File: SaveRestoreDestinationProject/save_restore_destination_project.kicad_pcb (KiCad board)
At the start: 2 copper layers, 21 parts

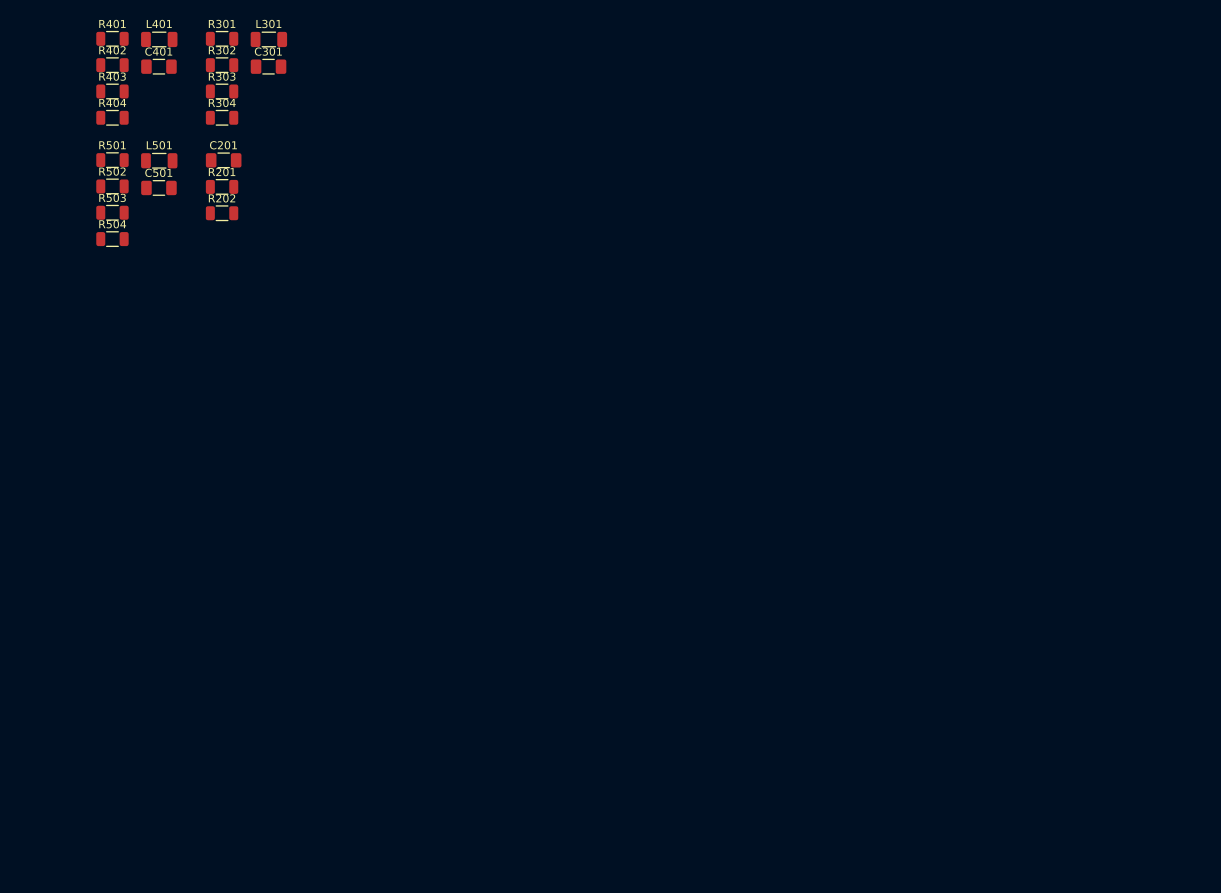
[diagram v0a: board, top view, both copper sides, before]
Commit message: Add support for connected drawings, update test template
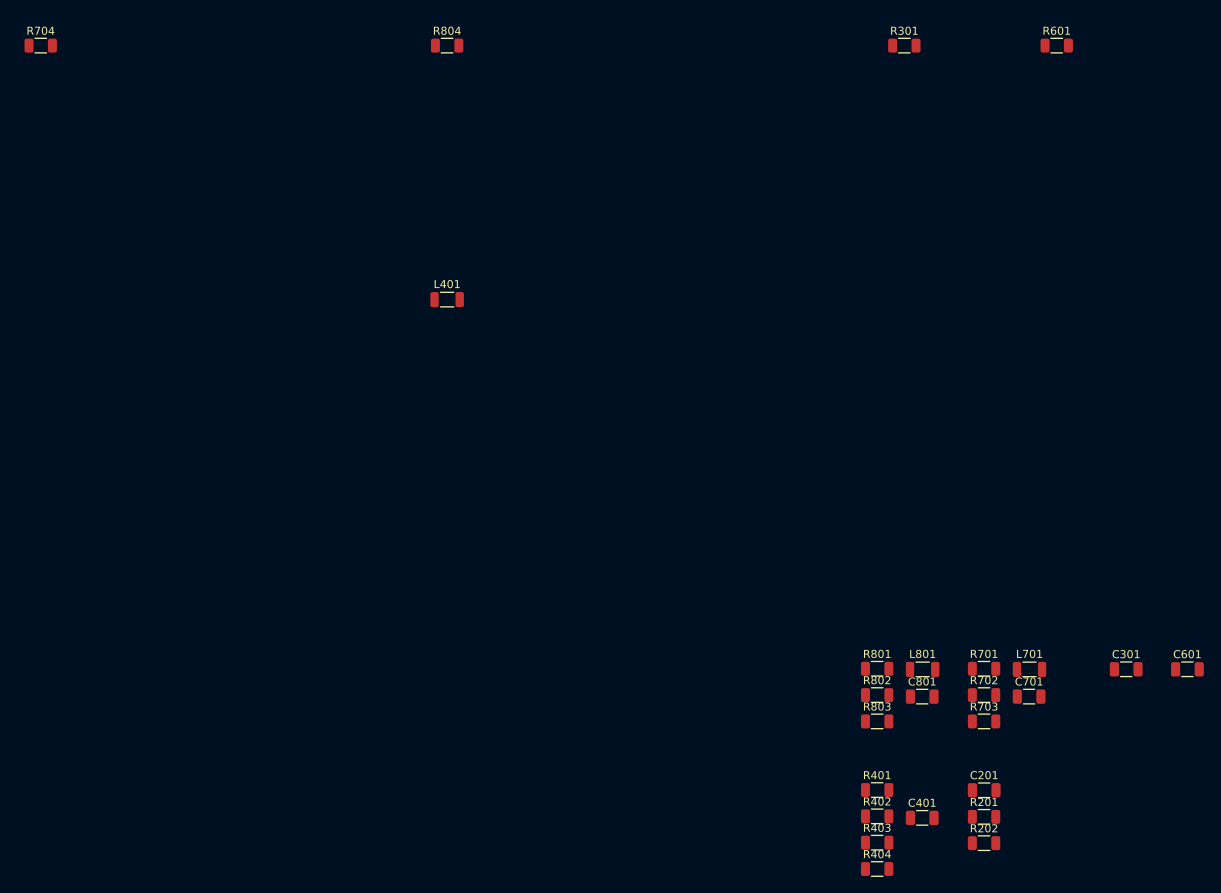
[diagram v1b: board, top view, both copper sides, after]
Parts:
- removed C501: 100n, Capacitor_SMD:C_1206_3216Metric_Pad1.33x1.80mm_HandSolder
- removed L301, L501: 10uH, Inductor_SMD:L_1206_3216Metric_Pad1.22x1.90mm_HandSolder
- removed R302, R502: 4k7, Resistor_SMD:R_1206_3216Metric
- removed R303, R503: 2k2, Resistor_SMD:R_1206_3216Metric
- removed R304, R501, R504: 1k, Resistor_SMD:R_1206_3216Metric
- added C601: C, Capacitor_SMD:C_1206_3216Metric, F.Cu at (219.5, 128.8)
- added C701: C, Capacitor_SMD:C_1206_3216Metric, F.Cu at (199.7, 132.2)
- added C801: C, Capacitor_SMD:C_1206_3216Metric, F.Cu at (186.4, 132.2)
- added L701: L, Inductor_SMD:L_1206_3216Metric, F.Cu at (199.8, 128.8)
- added L801: L, Inductor_SMD:L_1206_3216Metric, F.Cu at (186.4, 128.8)
- added R601: R, Resistor_SMD:R_1206_3216Metric, F.Cu at (203.2, 50.8)
- added R701: R, Resistor_SMD:R_1206_3216Metric, F.Cu at (194.1, 128.7)
- added R702: R, Resistor_SMD:R_1206_3216Metric, F.Cu at (194.1, 132.0)
- added R703: R, Resistor_SMD:R_1206_3216Metric, F.Cu at (194.1, 135.3)
- added R704: R, Resistor_SMD:R_1206_3216Metric, F.Cu at (76.2, 50.8)
- added R801: R, Resistor_SMD:R_1206_3216Metric, F.Cu at (180.8, 128.7)
- added R802: R, Resistor_SMD:R_1206_3216Metric, F.Cu at (180.8, 132.0)
- added R803: R, Resistor_SMD:R_1206_3216Metric, F.Cu at (180.8, 135.3)
- added R804: R, Resistor_SMD:R_1206_3216Metric, F.Cu at (127.0, 50.8)
- C201, C301, C401: value 100n -> C; footprint Capacitor_SMD:C_1206_3216Metric_Pad1.33x1.80mm_HandSolder -> Capacitor_SMD:C_1206_3216Metric
- L401: value 10uH -> L; footprint Inductor_SMD:L_1206_3216Metric_Pad1.22x1.90mm_HandSolder -> Inductor_SMD:L_1206_3216Metric
- R201, R202, R301, R401, R404: value 1k -> R
- R402: value 4k7 -> R
- R403: value 2k2 -> R
- moved R402 134.0 mm to (180.8, 147.1)
- moved R403 134.0 mm to (180.8, 150.4)
- moved R401 134.0 mm to (180.8, 143.9)
- moved R404 134.0 mm to (180.8, 153.7)
- moved C401 133.9 mm to (186.4, 147.3)
- moved C301 131.0 mm to (211.9, 128.8)
- moved R201 123.6 mm to (194.1, 147.2)
- moved R202 123.6 mm to (194.1, 150.5)
- moved C201 123.4 mm to (194.1, 143.9)
- moved R301 85.3 mm to (184.2, 50.8)
- moved L401 48.5 mm to (127.0, 82.5)
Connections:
- C201 pad 1: /Local1/local_2_a/out -> /local_1/local_2_a/out
- C201 pad 2: /Local1/local_2_b/in -> /local_1/local_2_b/in
- C301 pad 1: /Local1/local_2_a/out -> /relative_1/out
- C401 pad 1: /Local1/local_2_b/out -> /local_2/out
- L401 pad 2: Net-(L401-Pad2) -> /local_2/mid
- R201 pad 1: /Local1/local_2_a/in -> /local_1/in
- R201 pad 2: /Local1/in -> /local_1/local_2_a/in
- R202 pad 1: /Local1/out -> /local_1/local_2_b/out
- R202 pad 2: /Local1/local_2_b/out -> /local_1/out
- R301 pad 1: /Local1/local_2_a/in -> /relative_1/in
- R301 pad 2: Net-(L301-Pad1) -> /relative_1/out
- R401 pad 1: /Local1/local_2_b/in -> /local_2/in
- R403 pad 2: Net-(L401-Pad2) -> /local_2/mid
- R404 pad 1: /Local1/local_2_b/out -> /local_2/mid
- R404 pad 2: Net-(L401-Pad2) -> /local_2/out

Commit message: Change sorting and and find anchor fp with robust search
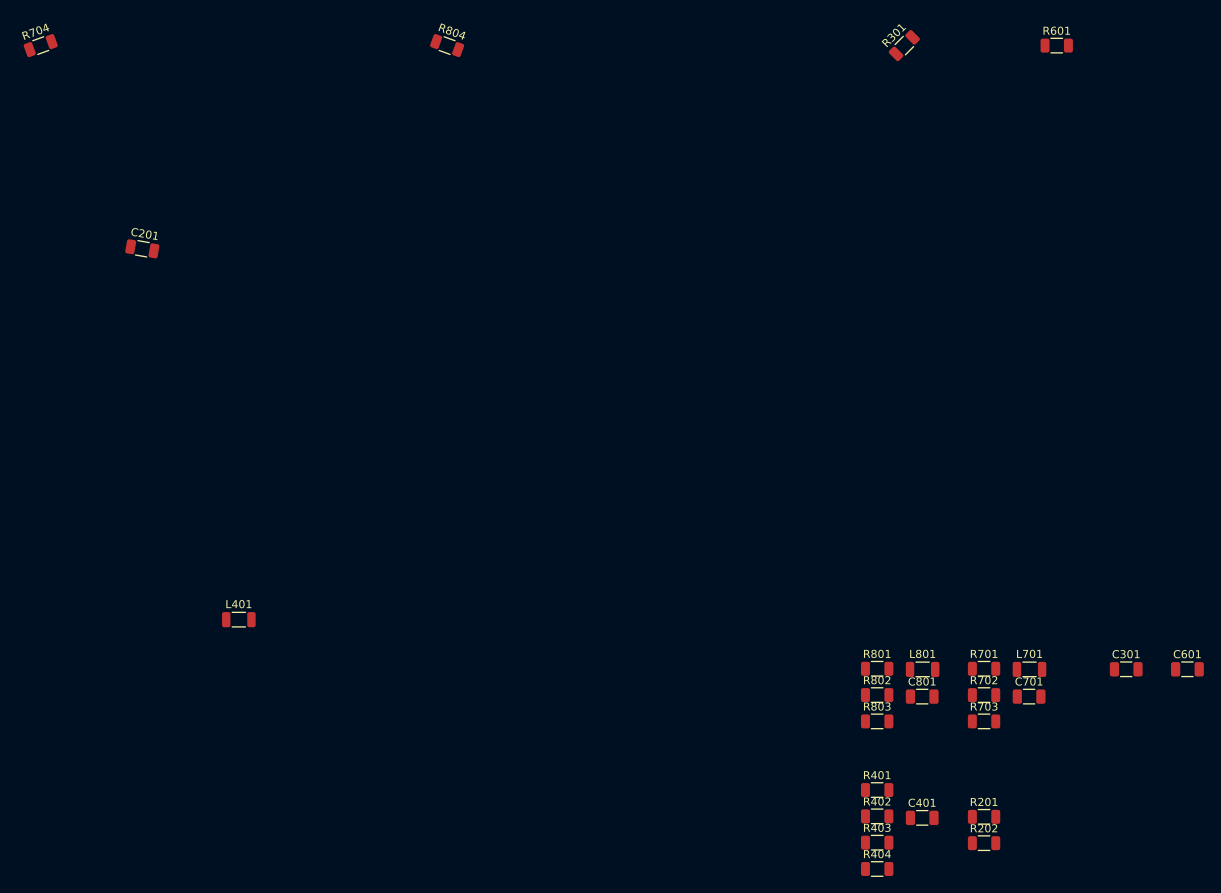
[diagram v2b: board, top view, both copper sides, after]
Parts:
- moved C201 125.1 mm to (88.9, 76.2), turned to -10 degrees
- moved L401 47.7 mm to (101.0, 122.6)
- turned R301 to 45 degrees
- turned R704 to 20 degrees
- turned R804 to -20 degrees
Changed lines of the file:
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@@
 	(footprint "Resistor_SMD:R_1206_3216Metric"
 		(layer "F.Cu")
-		(at 184.15 50.8)
+		(at 184.15 50.8 45)
 		(descr "Resistor SMD 1206 (3216 Metric), square (rectangular) end terminal, IPC_7351 nominal, (Body size source: IPC-SM-782 page 72, https://www.pcb-3d.com/wordpress/wp-content/uploads/ipc-sm-782a_amendment_1_and_2.pdf), generated with kicad-footprint-generator")
 		(tags "resistor")
 		(property "Reference" "R301"
-			(at 0 -1.82 0)
+			(at 0 -1.82 45)
 			(layer "F.SilkS")
 			(effects
@@
 		)
 		(property "Value" "R"
-			(at 0 1.82 0)
+			(at 0 1.82 45)
 			(layer "F.Fab")
 			(effects
@@
 		)
 		(property "Footprint" "Resistor_SMD:R_1206_3216Metric"
-			(at 0 0 0)
+			(at 0 0 45)
 			(unlocked yes)
 			(layer "F.Fab")
@@
 		)
 		(property "Datasheet" ""
-			(at 0 0 0)
+			(at 0 0 45)
 			(unlocked yes)
 			(layer "F.Fab")
@@
 		)
 		(property "Description" "Resistor"
-			(at 0 0 0)
+			(at 0 0 45)
 			(unlocked yes)
 			(layer "F.Fab")
@@
 		)
 		(fp_text user "${REFERENCE}"
-			(at 0 0 0)
+			(at 0 0 45)
 			(layer "F.Fab")
 			(effects
@@
 		)
 		(pad "1" smd roundrect
-			(at -1.4625 0)
+			(at -1.4625 0 45)
 			(size 1.125 1.75)
 			(layers "F.Cu" "F.Paste" "F.Mask")
@@
 		)
 		(pad "2" smd roundrect
-			(at 1.4625 0)
+			(at 1.4625 0 45)
 			(size 1.125 1.75)
 			(layers "F.Cu" "F.Paste" "F.Mask")
@@
 	(footprint "Resistor_SMD:R_1206_3216Metric"
 		(layer "F.Cu")
-		(at 127 50.8)
+		(at 127 50.8 -20)
 		(descr "Resistor SMD 1206 (3216 Metric), square (rectangular) end terminal, IPC_7351 nominal, (Body size source: IPC-SM-782 page 72, https://www.pcb-3d.com/wordpress/wp-content/uploads/ipc-sm-782a_amendment_1_and_2.pdf), generated with kicad-footprint-generator")
 		(tags "resistor")
 		(property "Reference" "R804"
-			(at 0 -1.82 0)
+			(at 0 -1.820001 160)
 			(layer "F.SilkS")
 			(effects
@@
 		)
 		(property "Value" "R"
-			(at 0 1.82 0)
+			(at 0 1.820001 160)
 			(layer "F.Fab")
 			(effects
@@
 		)
 		(property "Footprint" "Resistor_SMD:R_1206_3216Metric"
-			(at 0 0 0)
+			(at 0 0 -20)
 			(unlocked yes)
 			(layer "F.Fab")
@@
 		)
 		(property "Datasheet" ""
-			(at 0 0 0)
+			(at 0 0 -20)
 			(unlocked yes)
 			(layer "F.Fab")
@@
 		)
 		(property "Description" "Resistor"
-			(at 0 0 0)
+			(at 0 0 -20)
 			(unlocked yes)
 			(layer "F.Fab")
@@
 		(attr smd)
 		(fp_line
-			(start -0.727064 -0.91)
-			(end 0.727064 -0.91)
+			(start -0.727064 0.91)
+			(end 0.727064 0.91)
 			(stroke
 				(width 0.12)
@@
 		)
 		(fp_line
-			(start -0.727064 0.91)
-			(end 0.727064 0.91)
+			(start -0.727064 -0.91)
+			(end 0.727064 -0.91)
 			(stroke
 				(width 0.12)
@@
 		)
 		(fp_line
-			(start -2.28 -1.12)
-			(end 2.28 -1.12)
+			(start -2.28 1.12)
+			(end -2.28 -1.12)
 			(stroke
 				(width 0.05)
@@
 		)
 		(fp_line
-			(start -2.28 1.12)
-			(end -2.28 -1.12)
+			(start -2.28 -1.12)
+			(end 2.28 -1.12)
 			(stroke
 				(width 0.05)
@@
 		)
 		(fp_line
-			(start 2.28 -1.12)
-			(end 2.28 1.12)
+			(start 2.28 1.12)
+			(end -2.28 1.12)
 			(stroke
 				(width 0.05)
@@
 		)
 		(fp_line
-			(start 2.28 1.12)
-			(end -2.28 1.12)
+			(start 2.28 -1.12)
+			(end 2.28 1.12)
 			(stroke
 				(width 0.05)
@@
 		)
 		(fp_line
-			(start -1.6 -0.8)
-			(end 1.6 -0.8)
+			(start -1.6 0.8)
+			(end -1.6 -0.8)
 			(stroke
 				(width 0.1)
@@
 		)
 		(fp_line
-			(start -1.6 0.8)
-			(end -1.6 -0.8)
+			(start -1.6 -0.8)
+			(end 1.6 -0.8)
 			(stroke
 				(width 0.1)
@@
 		)
 		(fp_line
-			(start 1.6 -0.8)
-			(end 1.6 0.8)
+			(start 1.6 0.8)
+			(end -1.6 0.8)
 			(stroke
 				(width 0.1)
@@
 		)
 		(fp_line
-			(start 1.6 0.8)
-			(end -1.6 0.8)
+			(start 1.6 -0.8)
+			(end 1.6 0.8)
 			(stroke
 				(width 0.1)
@@
 		)
 		(fp_text user "${REFERENCE}"
-			(at 0 0 0)
+			(at 0 0 160)
 			(layer "F.Fab")
 			(effects
@@
 		)
 		(pad "1" smd roundrect
-			(at -1.4625 0)
+			(at -1.462499 0 340)
 			(size 1.125 1.75)
 			(layers "F.Cu" "F.Paste" "F.Mask")
@@
 		)
 		(pad "2" smd roundrect
-			(at 1.4625 0)
+			(at 1.462499 0 340)
 			(size 1.125 1.75)
 			(layers "F.Cu" "F.Paste" "F.Mask")
@@
 	(footprint "Resistor_SMD:R_1206_3216Metric"
 		(layer "F.Cu")
-		(at 76.2 50.8)
+		(at 76.2 50.8 20)
 		(descr "Resistor SMD 1206 (3216 Metric), square (rectangular) end terminal, IPC_7351 nominal, (Body size source: IPC-SM-782 page 72, https://www.pcb-3d.com/wordpress/wp-content/uploads/ipc-sm-782a_amendment_1_and_2.pdf), generated with kicad-footprint-generator")
 		(tags "resistor")
 		(property "Reference" "R704"
-			(at 0 -1.82 0)
+			(at 0 -1.820001 20)
 			(layer "F.SilkS")
 			(effects
@@
 		)
 		(property "Value" "R"
-			(at 0 1.82 0)
+			(at 0 1.820001 20)
 			(layer "F.Fab")
 			(effects
@@
 		)
 		(property "Footprint" "Resistor_SMD:R_1206_3216Metric"
-			(at 0 0 0)
+			(at 0 0 20)
 			(unlocked yes)
 			(layer "F.Fab")
@@
 		)
 		(property "Datasheet" ""
-			(at 0 0 0)
+			(at 0 0 20)
 			(unlocked yes)
 			(layer "F.Fab")
@@
 		)
 		(property "Description" "Resistor"
-			(at 0 0 0)
+			(at 0 0 20)
 			(unlocked yes)
 			(layer "F.Fab")
@@
 		)
 		(fp_text user "${REFERENCE}"
-			(at 0 0 0)
+			(at 0 0 20)
 			(layer "F.Fab")
 			(effects
@@
 		)
 		(pad "1" smd roundrect
-			(at -1.4625 0)
+			(at -1.462499 0 20)
 			(size 1.125 1.75)
 			(layers "F.Cu" "F.Paste" "F.Mask")
@@
 		)
 		(pad "2" smd roundrect
-			(at 1.4625 0)
+			(at 1.462499 0 20)
 			(size 1.125 1.75)
 			(layers "F.Cu" "F.Paste" "F.Mask")
@@
 	(footprint "Inductor_SMD:L_1206_3216Metric"
 		(layer "F.Cu")
-		(at 127 82.55)
+		(at 100.965 122.555)
 		(descr "Inductor SMD 1206 (3216 Metric), square (rectangular) end terminal, IPC_7351 nominal, (Body size source: IPC-SM-782 page 80, https://www.pcb-3d.com/wordpress/wp-content/uploads/ipc-sm-782a_amendment_1_and_2.pdf), generated with kicad-footprint-generator")
 		(tags "inductor")
@@
 	(footprint "Capacitor_SMD:C_1206_3216Metric"
 		(layer "F.Cu")
-		(at 194.1375 143.885)
+		(at 88.9 76.2 -10)
 		(descr "Capacitor SMD 1206 (3216 Metric), square (rectangular) end terminal, IPC_7351 nominal, (Body size source: IPC-SM-782 page 76, https://www.pcb-3d.com/wordpress/wp-content/uploads/ipc-sm-782a_amendment_1_and_2.pdf), generated with kicad-footprint-generator")
 		(tags "capacitor")
 		(property "Reference" "C201"
-			(at 0 -1.85 0)
+			(at 0 -1.85 170)
 			(layer "F.SilkS")
 			(effects
@@
 		)
 		(property "Value" "C"
-			(at 0 1.85 0)
+			(at 0 1.85 170)
 			(layer "F.Fab")
 			(effects
@@
 		)
 		(property "Footprint" "Capacitor_SMD:C_1206_3216Metric"
-			(at 0 0 0)
+			(at 0 0 -10)
 			(unlocked yes)
 			(layer "F.Fab")
@@
 		)
 		(property "Datasheet" ""
-			(at 0 0 0)
+			(at 0 0 -10)
 			(unlocked yes)
 			(layer "F.Fab")
@@
 		)
 		(property "Description" "Unpolarized capacitor"
-			(at 0 0 0)
+			(at 0 0 -10)
 			(unlocked yes)
 			(layer "F.Fab")
@@
 		(attr smd)
 		(fp_line
-			(start -0.711252 -0.91)
-			(end 0.711252 -0.91)
+			(start -0.711252 0.91)
+			(end 0.711252 0.91)
 			(stroke
 				(width 0.12)
@@
 		)
 		(fp_line
-			(start -0.711252 0.91)
-			(end 0.711252 0.91)
+			(start -0.711252 -0.91)
+			(end 0.711252 -0.91)
 			(stroke
 				(width 0.12)
@@
 		)
 		(fp_line
-			(start -2.3 -1.15)
-			(end 2.3 -1.15)
+			(start -2.3 1.15)
+			(end -2.3 -1.15)
 			(stroke
 				(width 0.05)
@@
 		)
 		(fp_line
-			(start -2.3 1.15)
-			(end -2.3 -1.15)
+			(start -2.3 -1.15)
+			(end 2.3 -1.15)
 			(stroke
 				(width 0.05)
@@
 		)
 		(fp_line
-			(start 2.3 -1.15)
-			(end 2.3 1.15)
+			(start 2.3 1.15)
+			(end -2.3 1.15)
 			(stroke
 				(width 0.05)
@@
 		)
 		(fp_line
-			(start 2.3 1.15)
-			(end -2.3 1.15)
+			(start 2.3 -1.15)
+			(end 2.3 1.15)
 			(stroke
 				(width 0.05)
@@
 		)
 		(fp_line
-			(start -1.6 -0.8)
-			(end 1.6 -0.8)
+			(start -1.6 0.8)
+			(end -1.6 -0.8)
 			(stroke
 				(width 0.1)
@@
 		)
 		(fp_line
-			(start -1.6 0.8)
-			(end -1.6 -0.8)
+			(start -1.6 -0.8)
+			(end 1.6 -0.8)
 			(stroke
 				(width 0.1)
@@
 		)
 		(fp_line
-			(start 1.6 -0.8)
-			(end 1.6 0.8)
+			(start 1.6 0.8)
+			(end -1.6 0.8)
 			(stroke
 				(width 0.1)
@@
 		)
 		(fp_line
-			(start 1.6 0.8)
-			(end -1.6 0.8)
+			(start 1.6 -0.8)
+			(end 1.6 0.8)
 			(stroke
 				(width 0.1)
@@
 		)
 		(fp_text user "${REFERENCE}"
-			(at 0 0 0)
+			(at 0 0 170)
 			(layer "F.Fab")
 			(effects
@@
 		)
 		(pad "1" smd roundrect
-			(at -1.475 0)
+			(at -1.475 0 350)
 			(size 1.15 1.8)
 			(layers "F.Cu" "F.Paste" "F.Mask")
@@
 		)
 		(pad "2" smd roundrect
-			(at 1.475 0)
+			(at 1.475 0 350)
 			(size 1.15 1.8)
 			(layers "F.Cu" "F.Paste" "F.Mask")
